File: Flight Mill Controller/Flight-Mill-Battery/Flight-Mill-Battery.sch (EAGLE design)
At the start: 219 parts, among them IC1 STM32G0B1RET6, IC10 SN65HVD3082EDR, IC11 TPS54202DDCR, IC12 LD117AS50TR, IC13 LD117AS33TR, IC2 CSTNE8M00G520000R0, IC3 MCP6001UT, IC4 LMV641, IC5 LMV641, IC6 LMV641, IC7 LMV641, IC8 LMV641, IC9 LMV641, J1 1050170001, J2 61300411121, J3 615008148521, J4 61300411121, K1 RYA31012, K2 RYA31012, Q1 BC817, Q2 UT2955G-AA3-R, Q3 2N7002, Q4 UT2955G-AA3-R, Q5 2N7002, Q6 UT2955G-AA3-R, Q7 2N7002, Q8 UT2955G-AA3-R, Q9 2N7002, X1 B2B-XH-AM(LF)(SN), X10 726386-2TE_726386-2, X11 726386-2TE_726386-2, X12 726386-2TE_726386-2, X13 726386-2TE_726386-2, X14 726386-2TE_726386-2, X15 726386-2TE_726386-2, X17 282834-3, X18 282834-3, X2 B2B-XH-AM(LF)(SN), X23 282834-2, X24 282834-3, X3 WF2549-2WS05S0B01, X4 282834-2, X5 726386-2TE_726386-2, X6 282834-2, X7 726386-2TE_726386-2, X8 5-102203-3, X9 5-102203-3

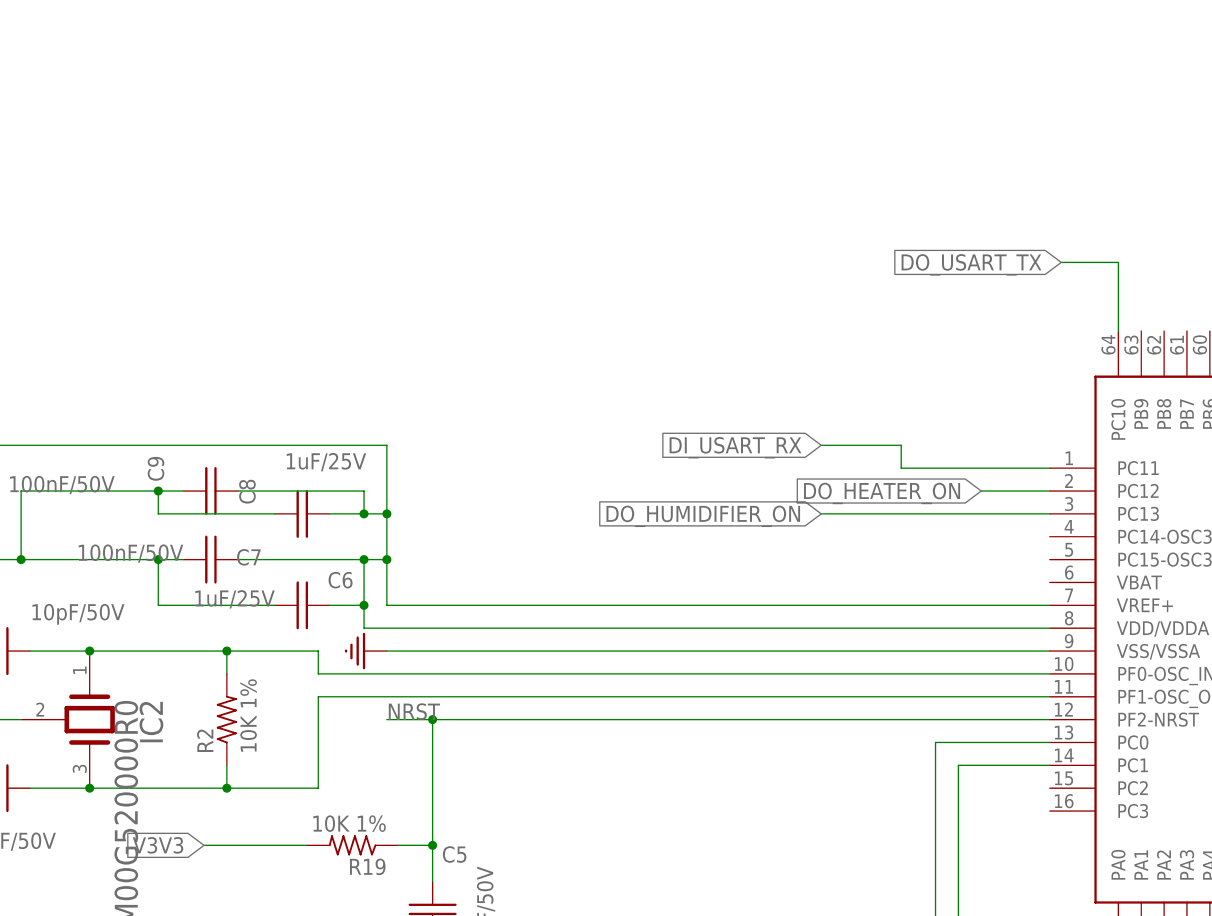
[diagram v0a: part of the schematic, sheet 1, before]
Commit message: HW00.00 Ongoing
Added Coin battery and 32KHz Crystal for RTC retention
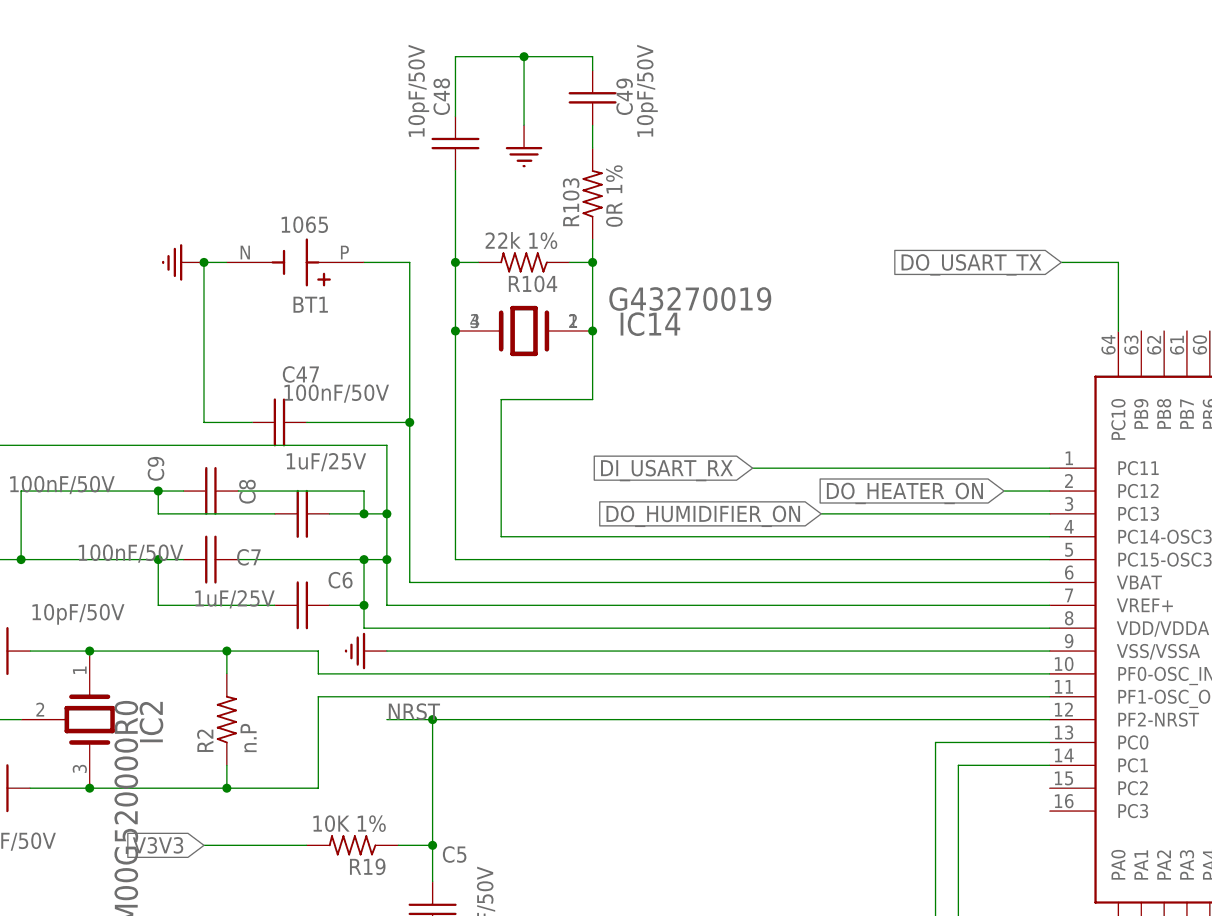
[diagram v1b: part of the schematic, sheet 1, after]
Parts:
- added BT1: 1065, Labops_Lib_AH:1065
- added C47: 100nF/50V, Labops_Lib_AH:C_0603EIA0603
- added C48, C49: 10pF/50V, Labops_Lib_AH:C_0603EIA0603
- added IC14: G43270019, Labops_Lib_AH:G43270019
- added R103: 0R 1%, Labops_Lib_AH:R_0603
- added R104: 22k 1%, Labops_Lib_AH:R_0603
- R2: value 10K 1% -> n.P
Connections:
- new net N$65: BT1.POS, C47.1, IC1.VBAT
- new net N$67: C48.1, IC1.PC15-OSC32_OUT, IC14.3, IC14.4, R104.2
- new net N$69: IC1.PC14-OSC32_IN, IC14.1, IC14.2, R103.1, R104.1
- new net N$72: C49.1, R103.2
- net GND: now also BT1.NEG, C47.2, C48.2, C49.2
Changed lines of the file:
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@@
 <setting verticaltext="up"/>
 </settings>
-<grid distance="0.05" unitdist="inch" unit="inch" style="lines" multiple="1" display="yes" altdistance="0.01" altunitdist="inch" altunit="inch"/>
+<grid distance="0.1" unitdist="inch" unit="inch" style="lines" multiple="1" display="yes" altdistance="0.01" altunitdist="inch" altunit="inch"/>
 <layers>
 <layer number="1" name="Top" color="4" fill="1" visible="no" active="no"/>
@@
 <part name="R1" library="Labops_Lib_AH" deviceset="R_0603" device="" value="100K 1%"/>
 <part name="IC2" library="Labops_Lib_AH" deviceset="CSTNE8M00G520000R0" device=""/>
-<part name="R2" library="Labops_Lib_AH" deviceset="R_0603" device="" value="10K 1%"/>
+<part name="R2" library="Labops_Lib_AH" deviceset="R_0603" device="" value="n.P"/>
 <part name="C1" library="Labops_Lib_AH" deviceset="C_0603" device="EIA0603" value="10pF/50V"/>
 <part name="C2" library="Labops_Lib_AH" deviceset="C_0603" device="EIA0603" value="10pF/50V"/>
@@
 <part name="C45" library="Labops_Lib_AH" deviceset="C_0603" device="EIA0603" value="100nF 100V"/>
 <part name="C46" library="Labops_Lib_AH" deviceset="C_0603" device="EIA0603" value="1uF/35V"/>
+<part name="BT1" library="Labops_Lib_AH" deviceset="1065" device=""/>
+<part name="GND71" library="Labops_Lib_AH" deviceset="GND" device=""/>
+<part name="C47" library="Labops_Lib_AH" deviceset="C_0603" device="EIA0603" value="100nF/50V"/>
+<part name="IC14" library="Labops_Lib_AH" deviceset="G43270019" device=""/>
+<part name="R103" library="Labops_Lib_AH" deviceset="R_0603" device="" value="0R 1%"/>
+<part name="C48" library="Labops_Lib_AH" deviceset="C_0603" device="EIA0603" value="10pF/50V"/>
+<part name="C49" library="Labops_Lib_AH" deviceset="C_0603" device="EIA0603" value="10pF/50V"/>
+<part name="GND72" library="Labops_Lib_AH" deviceset="GND" device=""/>
+<part name="R104" library="Labops_Lib_AH" deviceset="R_0603" device="" value="22k 1%"/>
 </parts>
 <sheets>
@@
 <attribute name="NAME" x="75.692" y="13.2842" size="1.778" layer="95"/>
 <attribute name="VALUE" x="75.692" y="10.2362" size="1.778" layer="96"/>
+</instance>
+<instance part="BT1" gate="G$1" x="58.42" y="231.14" smashed="yes" rot="R180">
+<attribute name="NAME" x="62.23" y="227.33" size="1.778" layer="95" rot="R180"/>
+<attribute name="VALUE" x="62.23" y="236.22" size="1.778" layer="96" rot="R180"/>
+</instance>
+<instance part="GND71" gate="1" x="45.72" y="231.14" smashed="yes" rot="R270"/>
+<instance part="C47" gate="G$1" x="57.15" y="213.36" smashed="yes" rot="R270">
+<attribute name="NAME" x="56.896" y="217.805" size="1.778" layer="95"/>
+<attribute name="VALUE" x="68.834" y="217.551" size="1.778" layer="96" rot="R180"/>
+</instance>
+<instance part="IC14" gate="G$1" x="88.9" y="215.9" smashed="yes" rot="R180">
+<attribute name="NAME" x="101.346" y="223.012" size="2.54" layer="95" rot="R180" align="top-left"/>
+<attribute name="VALUE" x="111.506" y="225.806" size="2.54" layer="95" rot="R180" align="top-left"/>
+</instance>
+<instance part="R103" gate="G$1" x="91.44" y="238.76" smashed="yes" rot="R90">
+<attribute name="NAME" x="89.9414" y="234.95" size="1.778" layer="95" rot="R90"/>
+<attribute name="VALUE" x="94.742" y="234.95" size="1.778" layer="96" rot="R90"/>
+</instance>
+<instance part="C48" gate="G$1" x="76.2" y="243.84" smashed="yes" rot="R180">
+<attribute name="NAME" x="75.565" y="247.396" size="1.778" layer="95" rot="R90"/>
+<attribute name="VALUE" x="72.771" y="244.856" size="1.778" layer="96" rot="R90"/>
+</instance>
+<instance part="C49" gate="G$1" x="91.44" y="248.92" smashed="yes" rot="R180">
+<attribute name="NAME" x="95.885" y="247.396" size="1.778" layer="95" rot="R90"/>
+<attribute name="VALUE" x="98.171" y="244.856" size="1.778" layer="96" rot="R90"/>
+</instance>
+<instance part="GND72" gate="1" x="83.82" y="243.84" smashed="yes"/>
+<instance part="R104" gate="G$1" x="83.82" y="231.14" smashed="yes" rot="R180">
+<attribute name="NAME" x="87.63" y="229.6414" size="1.778" layer="95" rot="R180"/>
+<attribute name="VALUE" x="87.63" y="234.442" size="1.778" layer="96" rot="R180"/>
 </instance>
 </instances>
@@
 <junction x="152.4" y="121.92"/>
 </segment>
+<segment>
+<pinref part="GND71" gate="1" pin="GND"/>
+<pinref part="BT1" gate="G$1" pin="NEG"/>
+<wire x1="48.26" y1="231.14" x2="50.8" y2="231.14" width="0.1524" layer="91"/>
+<pinref part="C47" gate="G$1" pin="2"/>
+<wire x1="53.594" y1="213.36" x2="48.26" y2="213.36" width="0.1524" layer="91"/>
+<wire x1="48.26" y1="213.36" x2="48.26" y2="231.14" width="0.1524" layer="91"/>
+<junction x="48.26" y="231.14"/>
+</segment>
+<segment>
+<pinref part="C48" gate="G$1" pin="2"/>
+<wire x1="76.2" y1="247.396" x2="76.2" y2="254" width="0.1524" layer="91"/>
+<wire x1="76.2" y1="254" x2="83.82" y2="254" width="0.1524" layer="91"/>
+<pinref part="GND72" gate="1" pin="GND"/>
+<wire x1="83.82" y1="254" x2="83.82" y2="246.38" width="0.1524" layer="91"/>
+<pinref part="C49" gate="G$1" pin="2"/>
+<wire x1="91.44" y1="252.476" x2="91.44" y2="254" width="0.1524" layer="91"/>
+<wire x1="91.44" y1="254" x2="83.82" y2="254" width="0.1524" layer="91"/>
+<junction x="83.82" y="254"/>
+</segment>
 </net>
 <net name="USB_DM" class="0">
@@
 <segment>
 <pinref part="IC1" gate="G$1" pin="PC12"/>
-<wire x1="142.24" y1="205.74" x2="134.62" y2="205.74" width="0.1524" layer="91"/>
-<label x="134.62" y="205.74" size="1.778" layer="95" rot="R180" xref="yes"/>
+<wire x1="142.24" y1="205.74" x2="137.16" y2="205.74" width="0.1524" layer="91"/>
+<label x="137.16" y="205.74" size="1.778" layer="95" rot="R180" xref="yes"/>
 </segment>
 </net>
@@
 <segment>
 <pinref part="IC1" gate="G$1" pin="PC11"/>
-<wire x1="142.24" y1="208.28" x2="125.73" y2="208.28" width="0.1524" layer="91"/>
-<label x="116.84" y="210.82" size="1.778" layer="95" rot="R180" xref="yes"/>
-<wire x1="116.84" y1="210.82" x2="125.73" y2="210.82" width="0.1524" layer="91"/>
-<wire x1="125.73" y1="210.82" x2="125.73" y2="208.28" width="0.1524" layer="91"/>
+<label x="109.22" y="208.28" size="1.778" layer="95" rot="R180" xref="yes"/>
+<wire x1="109.22" y1="208.28" x2="142.24" y2="208.28" width="0.1524" layer="91"/>
 </segment>
 </net>
@@
 </segment>
 </net>
+<net name="N$65" class="0">
+<segment>
+<pinref part="BT1" gate="G$1" pin="POS"/>
+<wire x1="66.04" y1="231.14" x2="71.12" y2="231.14" width="0.1524" layer="91"/>
+<wire x1="71.12" y1="231.14" x2="71.12" y2="213.36" width="0.1524" layer="91"/>
+<wire x1="71.12" y1="213.36" x2="71.12" y2="195.58" width="0.1524" layer="91"/>
+<pinref part="IC1" gate="G$1" pin="VBAT"/>
+<wire x1="71.12" y1="195.58" x2="142.24" y2="195.58" width="0.1524" layer="91"/>
+<pinref part="C47" gate="G$1" pin="1"/>
+<wire x1="59.69" y1="213.36" x2="71.12" y2="213.36" width="0.1524" layer="91"/>
+<junction x="71.12" y="213.36"/>
+</segment>
+</net>
+<net name="N$67" class="0">
+<segment>
+<pinref part="IC14" gate="G$1" pin="3"/>
+<wire x1="76.2" y1="223.52" x2="76.2" y2="198.12" width="0.1524" layer="91"/>
+<pinref part="IC1" gate="G$1" pin="PC15-OSC32_OUT"/>
+<wire x1="76.2" y1="198.12" x2="142.24" y2="198.12" width="0.1524" layer="91"/>
+<pinref part="IC14" gate="G$1" pin="4"/>
+<junction x="76.2" y="223.52"/>
+<pinref part="C48" gate="G$1" pin="1"/>
+<wire x1="76.2" y1="223.52" x2="76.2" y2="231.14" width="0.1524" layer="91"/>
+<pinref part="R104" gate="G$1" pin="2"/>
+<wire x1="76.2" y1="231.14" x2="76.2" y2="241.3" width="0.1524" layer="91"/>
+<wire x1="78.74" y1="231.14" x2="76.2" y2="231.14" width="0.1524" layer="91"/>
+<junction x="76.2" y="231.14"/>
+</segment>
+</net>
+<net name="N$69" class="0">
+<segment>
+<pinref part="IC1" gate="G$1" pin="PC14-OSC32_IN"/>
+<wire x1="142.24" y1="200.66" x2="81.28" y2="200.66" width="0.1524" layer="91"/>
+<wire x1="81.28" y1="200.66" x2="81.28" y2="215.9" width="0.1524" layer="91"/>
+<wire x1="81.28" y1="215.9" x2="91.44" y2="215.9" width="0.1524" layer="91"/>
+<pinref part="IC14" gate="G$1" pin="1"/>
+<wire x1="91.44" y1="215.9" x2="91.44" y2="223.52" width="0.1524" layer="91"/>
+<pinref part="IC14" gate="G$1" pin="2"/>
+<junction x="91.44" y="223.52"/>
+<pinref part="R103" gate="G$1" pin="1"/>
+<wire x1="91.44" y1="233.68" x2="91.44" y2="231.14" width="0.1524" layer="91"/>
+<pinref part="R104" gate="G$1" pin="1"/>
+<wire x1="91.44" y1="231.14" x2="91.44" y2="223.52" width="0.1524" layer="91"/>
+<wire x1="88.9" y1="231.14" x2="91.44" y2="231.14" width="0.1524" layer="91"/>
+<junction x="91.44" y="231.14"/>
+</segment>
+</net>
+<net name="N$72" class="0">
+<segment>
+<pinref part="C49" gate="G$1" pin="1"/>
+<pinref part="R103" gate="G$1" pin="2"/>
+<wire x1="91.44" y1="246.38" x2="91.44" y2="243.84" width="0.1524" layer="91"/>
+</segment>
+</net>

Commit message: HW01
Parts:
- removed C20, C21: 100nF/50V, Labops_Lib_AH:C_0603EIA0603
- removed IC9: LMV641, Labops_Lib_AH:LMV641
- removed R103, R44, R58: 0R 1%, Labops_Lib_AH:R_0603
- removed R43, R56, R57: 100R 1%, Labops_Lib_AH:R_0603
- removed R54, R55: 1.5K 1%, Labops_Lib_AH:R_0603
- added C50, C51, C52: 100nF/50V, Labops_Lib_AH:C_0603EIA0603
- added IC15: LMV641, Labops_Lib_AH:LMV641
- added R105: 10R 1%, Labops_Lib_AH:R_0603
- added R106, R107: 2.49K 1%, Labops_Lib_AH:R_0603
- C11, C17: value 100nF/50V -> 0R 1%
- C15, C19: value 100nF/50V -> 10pF/50V
- C25: value (none) -> 100nF
- C35: value 100nF 100V -> 100pF 100V
- R14: value 47K 1% -> 100K 1%
- R22, R84: value 10k 1% -> 100R 1%
- R33, R34: value 10K 1% -> 100R 1%
- R39, R53: value 10K 1% -> n.P
- R40: value 1.5K 1% -> 10R 1%
- R41: value 100R 1% -> 2.49KK 1%
- R42: value 1.5K 1% -> 2.49K 1%
- R52: value 10K 1% -> 10k 1%
- R9: value 330R 1% -> 33R 1%
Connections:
- removed net N$22: IC6.OUT@1, R44.2
- removed net N$28: IC9.IN+, R57.2
- removed net N$29: IC9.IN-, R56.2
- removed net N$30: C20.1, R55.2, R56.1
- removed net N$31: IC9.OUT@1, R58.2
- removed net VREF_O2: IC4.IN+, IC7.IN+, R31.2, R32.1, R36.2, R42.1, R45.2, R46.1, R50.2, R55.1
- new net N$70: IC15.IN-, R105.2
- new net N$71: IC15.OUT@1, R105.1, R50.2
- new net VREF_O2_1: C51.2, IC7.IN+, R45.2, R46.1
- new net VREF_O2_2: IC4.IN+, R31.2, R32.1
- net AI_O2_SENSOR: no longer R40.1
- net AI_O2_SENSOR1: no longer R44.1
- net AI_O2_SENSOR2: no longer R58.1
- net GND: now also C14.1, C50.2, C51.1, C52.1, IC10.GND, IC15.VEE@2, R106.2, R41.2; no longer C14.2, C15.2, C19.1, C20.2, C21.2, IC9.VEE@2
- net N$15: now also IC6.IN-; no longer C13.2, R41.1
- net N$18: now also IC6.OUT@1, R36.2, R40.1; no longer IC6.IN+, R41.2
- net N$20: now also C19.2, C48.1; no longer IC6.IN-, R43.2
- net N$21: now also C13.2, IC6.IN+, R41.1, R42.1; no longer C14.1, R42.2, R43.1
- net N$27: now also C52.2, IC15.IN+, R106.1, R107.1; no longer C19.2, R54.2, R57.1
- net N$32: no longer R54.1
- net N$67: now also C19.1; no longer C48.1
- net N$69: now also C15.1; no longer R103.1
- net N$72: now also C15.2; no longer R103.2
- net V5V0: now also C14.2, C50.1, IC15.VCC@5, R107.2, R42.2; no longer C15.1, C21.1, IC9.VCC@5
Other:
- moved on the sheet: C12, C13, C14, C48, IC6, R35, R36, R38, R40, R41, R42
